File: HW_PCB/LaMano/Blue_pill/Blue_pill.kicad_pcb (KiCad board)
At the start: 2 copper layers, 38.6 x 55.1 mm, 28 parts, among them J1 V_Battery, J2 STLINK, J5 MPU6050, J6 NRF24, SW1 SW_DPST_x2, SW2 SW_DPST_x2, U1 STM32F103C8Tx, U2 AMS1117-3.3, X1 Crystal

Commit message: HAND FULL
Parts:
- SW1: footprint Button_Switch_SMD:SW_MEC_5GSH9 -> SWESPECIAL:SWESPECIAL
- moved SW1 17.3 mm to (56.3, 74.3)
- moved C2 3.14 mm to (51.6, 68.7), turned to -90 degrees
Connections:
- C7 pad 1: Net-(U2-VI) -> VIN
- U2 pad 3: Net-(U2-VI) -> VIN
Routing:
- net GND: track 69.8 -> 112.6 mm
- net ADC1: track 37.4 -> 0.00 mm
- net VCC: track 127.9 -> 110.8 mm
- net NRST: track 15.8 -> 23.7 mm
- net SWCLK: track 7.11 -> 7.65 mm
- added copper zone on F.Cu, net GND

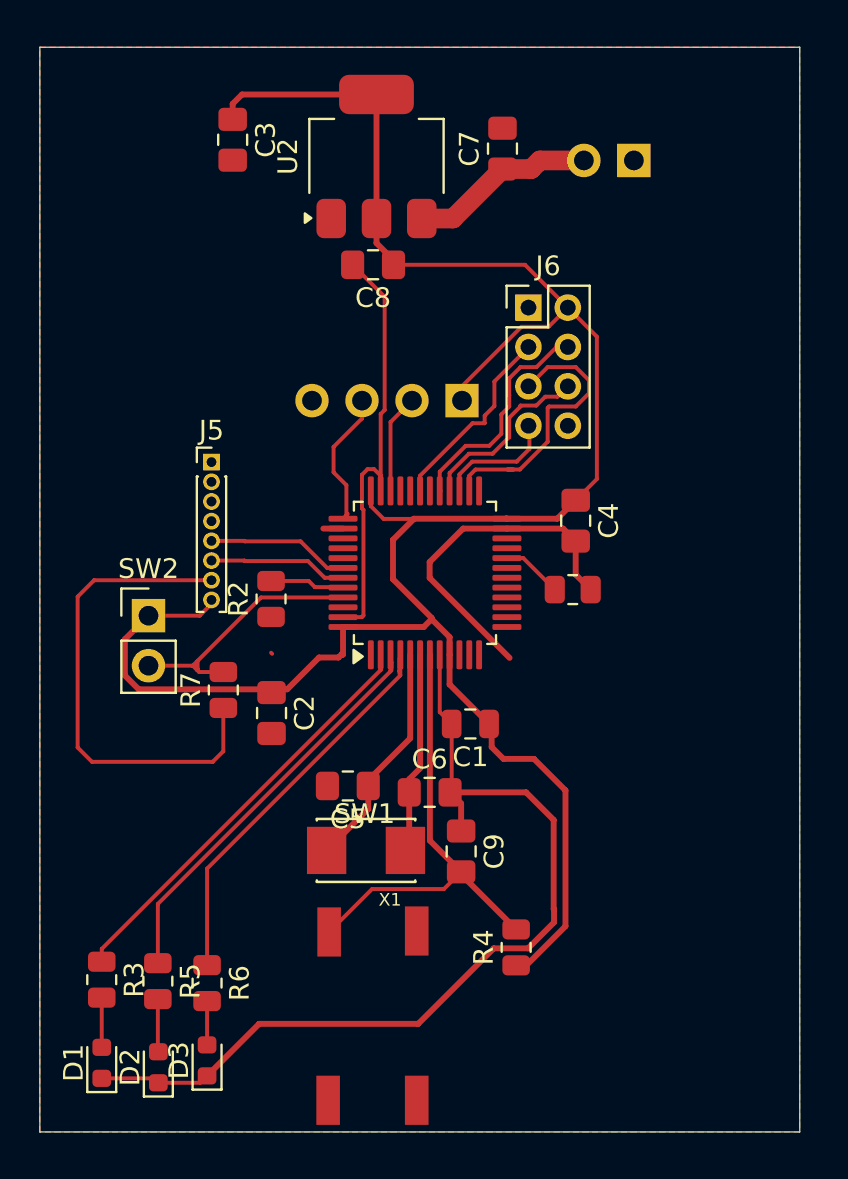
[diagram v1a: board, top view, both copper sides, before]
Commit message: Rearranged components
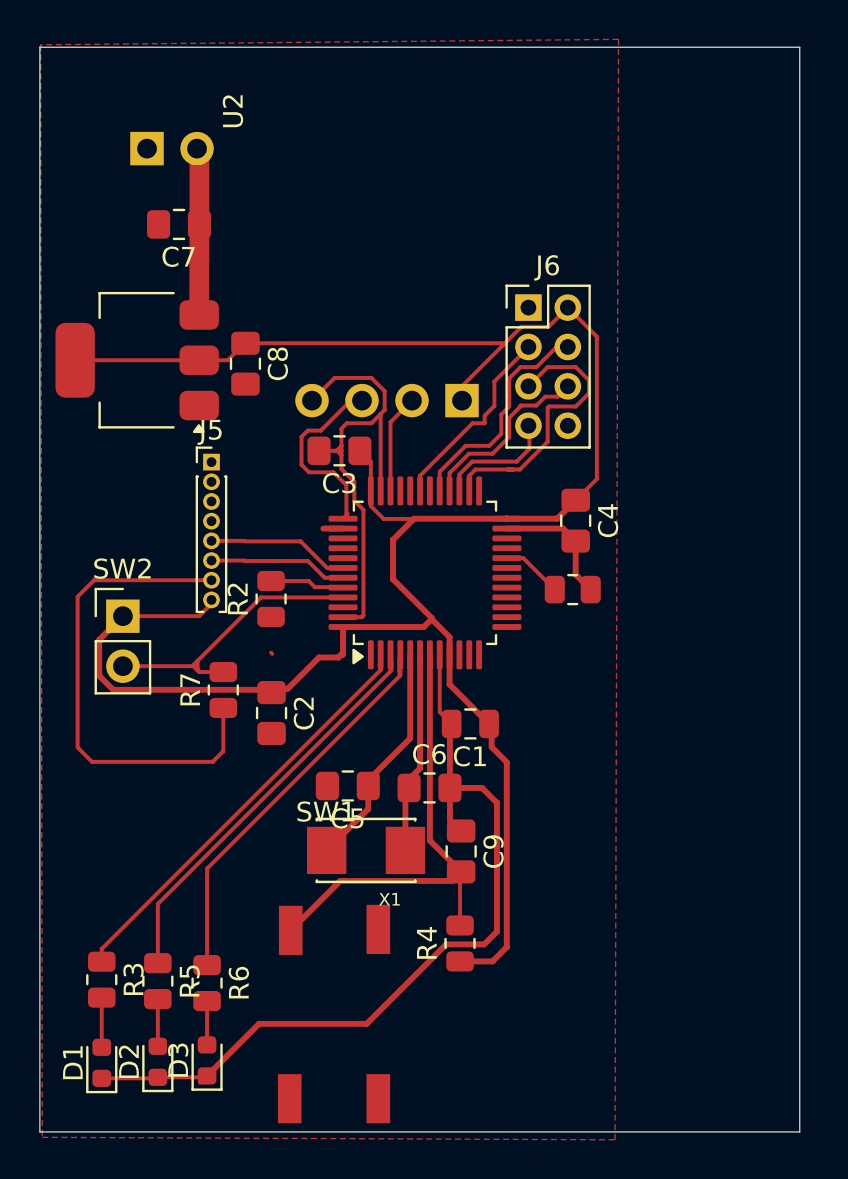
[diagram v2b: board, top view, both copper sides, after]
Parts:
- moved J1 24.7 mm to (45.3, 40.0), turned to -90 degrees
- moved C7 16.9 mm to (46.9, 43.9), turned to 180 degrees
- moved C3 16.7 mm to (55.0, 55.4), turned to 180 degrees
- moved U2 16.0 mm to (44.8, 50.8), turned to 180 degrees
- moved C8 8.20 mm to (50.3, 50.9), turned to -90 degrees
- moved R4 2.86 mm to (61.2, 80.4)
- moved SW1 1.95 mm to (54.4, 74.2)
- moved SW2 1.30 mm to (44.0, 63.8)
- moved D2 0.28 mm to (45.8, 86.4)
- moved C6 0.23 mm to (59.6, 72.5)
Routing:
- net GND: track 112.6 -> 99.5 mm
- net SWCLK: track 7.65 -> 10.4 mm
- net VCC: track 110.8 -> 108.9 mm
- net SW_LUZ: track 13.5 -> 14.8 mm
- net VIN: track 9.46 -> 8.51 mm
- net NRST: track 23.7 -> 24.5 mm
